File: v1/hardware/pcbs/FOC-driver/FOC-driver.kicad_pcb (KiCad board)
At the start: 4 copper layers, 100 x 100 mm, 225 parts, among them J1 HB9500M-9.5-2P, J10 S4B-XH-A, J11 S10B-XH-A, J12 S8B-XH-A, J13 S5B-XH-A, J14 S2B-XH-A, J16 S2B-XH-A, J2 HB9500-3, J3 B2B-XH-A, J4 B2B-XH-A, J5 B2B-XH-A, J6 B2B-XH-A, J7 S2B-XH-A, J8 S5B-XH-A, J9 S4B-XH-A, Q1 BSC093N15NS5, Q10 40N05, Q11 40N05, Q2 BSC093N15NS5, Q3 BSC093N15NS5, Q4 BSC093N15NS5, Q5 BSC093N15NS5, Q6 BSC093N15NS5, Q7 SP015N03BGHTO, Q8 40N05, Q9 40N05, SW1 TS-1088-AR02016, SW2 MSK22D18G2 125, Y1 C19674287, Y2 C48615

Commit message: new FOC driver connector placements and labels
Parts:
- removed LED3, LED4: C965799, LED_SMD:LED_0603_1608Metric
- removed R68: 300, Resistor_SMD:R_0402_1005Metric
- added J15: S5B-XH-A, Connector_JST:JST_XH_S5B-XH-A_1x05_P2.50mm_Horizontal, F.Cu at (-40.5, 28.0)
- R55: value 300 -> 10K
- moved F1 156.9 mm to (-42.0, -20.0)
- moved C37 150.2 mm to (-29.8, -28.0), turned to -90 degrees
- moved R55 85.9 mm to (-136.0, 154.6)
- moved C1 52.1 mm to (-152.8, -7.40)
- moved C14 52.1 mm to (-174.5, 136.1)
- moved C15 52.1 mm to (-174.5, 138.1)
- moved C19 52.1 mm to (-130.1, 120.6)
- moved C22 52.1 mm to (-138.0, 117.2)
- moved C23 52.1 mm to (-138.0, 122.1)
- moved C24 52.1 mm to (-163.5, 91.6)
- moved C25 52.1 mm to (-163.5, 93.6)
- moved C26 52.1 mm to (-130.1, 143.1)
- moved C27 52.1 mm to (-163.5, 95.6)
- moved C28 52.1 mm to (-163.5, 97.5)
- moved C29 52.1 mm to (-138.0, 139.6)
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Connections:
- net /LED1 renamed /LED
- MCU1 pad 26: /FAN2.EN -> /FAN1.EN
- MCU1 pad 30: /FAN3.PWM -> /DIP.CONF0
- MCU1 pad 33: /FAN4.PWM -> /DIP.CONF1
- MCU1 pad 34: /FAN4.EN -> /DIP.CONF2
- MCU1 pad 39: /DIP.CONF0 -> /FAN2.PWM
- MCU1 pad 40: /DIP.CONF1 -> /FAN3.PWM
- MCU1 pad 41: /DIP.CONF2 -> /FAN4.PWM
- MCU1 pad 49: /FDCAN.SILENT -> /DEBUG.SWDIO
- MCU1 pad 50: /FAN1.EN -> /DEBUG.SWCLK
- MCU1 pad 52: /LED3 -> /FAN4.EN
- MCU1 pad 53: /ENDSTOP1 -> /FAN3.EN
- MCU1 pad 54: /ENDSTOP2 -> /FAN2.EN
- MCU1 pad 56: /FAN2.PWM -> /DEBUG.SWO
- MCU1 pad 62: /FAN3.EN -> /ENDSTOP2
- MCU1 pad 8: /LED2 -> /ENDSTOP1
- R54 pad 1: /LED2 -> +3.3V
- R55 pad 1: /LED3 -> /FDCAN.SILENT
- R55 pad 2: Net-(LED3-A) -> GND
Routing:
- net GND: track 1.05 -> 15.1 mm, vias 1 -> 5
- net /power/VMOT_UNFUSED: track 11.3 -> 23.4 mm
- net /power/VMOT_UNFILTERED: track 9.73 -> 3.17 mm
- net /power/VMOT_GATE: track 11.6 -> 12.5 mm
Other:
- board text added: "+"
- board text added: "-"
- board text added: "- FAN +"
- board text added: "GND 5V A+A- B+B- Z+Z- ENCODER ABZ"
- board text added: "GND 5V CK+CK- CS+CS- MO+MO- MI+MI- ENCODER SPI"
- board text added: "GND 5V S+S- ENDSTOP1"
- board text added: "GND 5V S+S- ENDSTOP2"
- board text added: "GND CAN+CAN- CAN-CAN+ CAN-FD"
- board text added: "GND NRST CLK DIO SWO SW DEBUG"
- board text added: "GND TX+TX- RX+RX- RS422"
- board text added: "MOTOR TH"

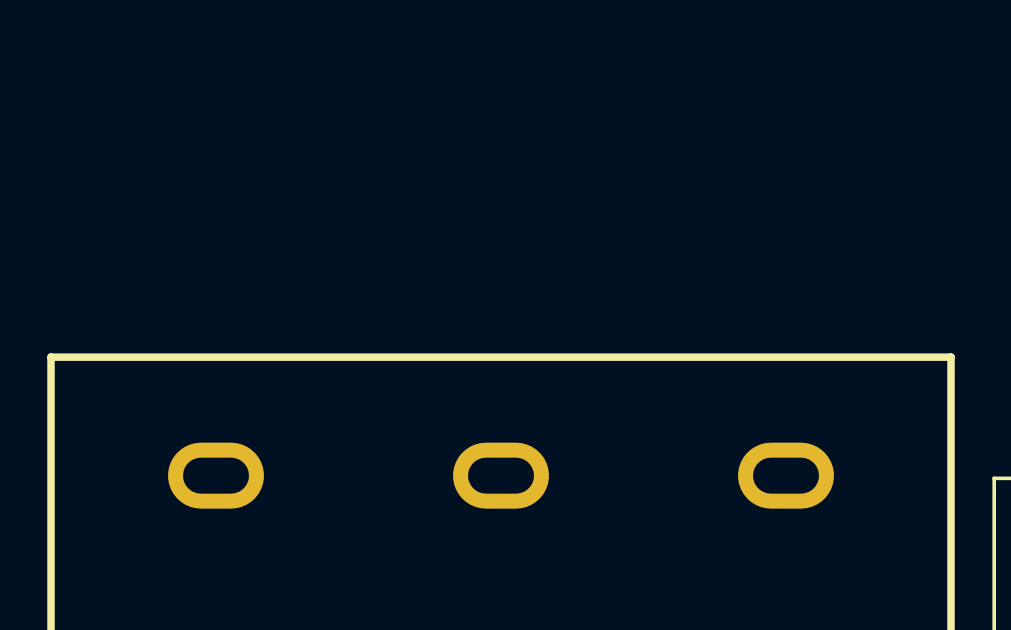
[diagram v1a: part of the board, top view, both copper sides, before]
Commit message: new FOC driver inverter out label
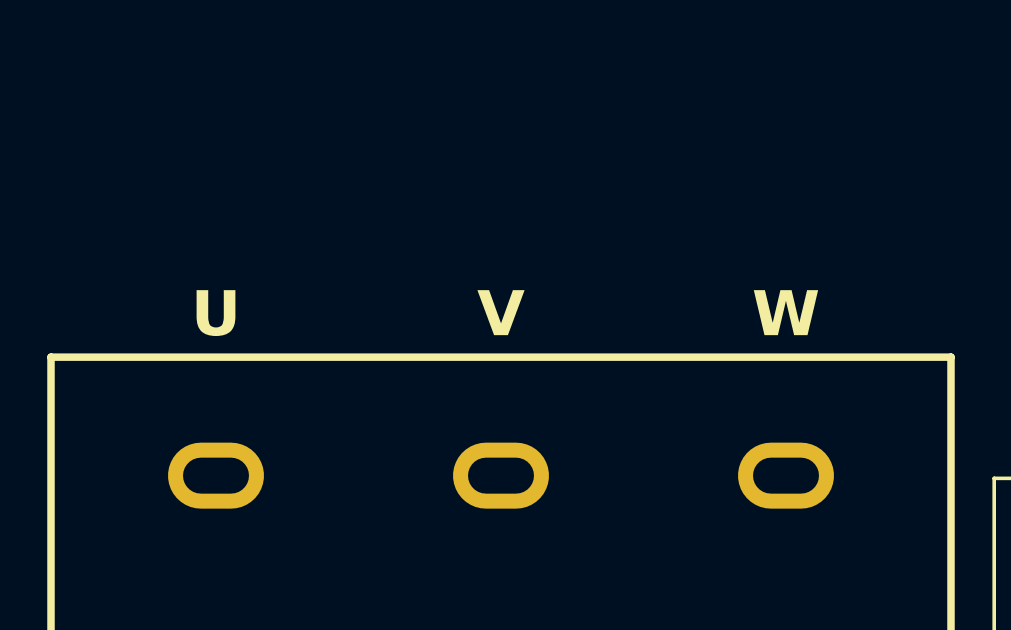
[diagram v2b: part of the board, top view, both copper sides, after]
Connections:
- J2 pad 1: /W_POWER -> /U_POWER
- J2 pad 3: /U_POWER -> /W_POWER
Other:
- board text added: "U"
- board text added: "V"
- board text added: "W"
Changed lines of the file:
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@@
 			(layers "*.Cu" "*.Mask")
 			(remove_unused_layers no)
-			(net 32 "/W_POWER")
+			(net 30 "/U_POWER")
 			(pinfunction "1")
 			(pintype "passive")
@@
 			(layers "*.Cu" "*.Mask")
 			(remove_unused_layers no)
-			(net 30 "/U_POWER")
+			(net 32 "/W_POWER")
 			(pinfunction "3")
 			(pintype "passive")
@@
 		(layer "Edge.Cuts")
 	)
+	(gr_text "V"
+		(at -2 33.5 0)
+		(layer "F.SilkS")
+		(effects
+			(font
+				(size 1.5 1.5)
+				(thickness 0.3)
+				(bold yes)
+			)
+			(justify bottom)
+		)
+	)
 	(gr_text "GND 5V A+A- B+B- Z+Z-\nENCODER ABZ"
 		(at 39 24.75 90)
@@
 				(bold yes)
 			)
+			(justify bottom)
+		)
+	)
+	(gr_text "W"
+		(at 7.5 33.5 0)
+		(layer "F.SilkS")
+		(effects
+			(font
+				(size 1.5 1.5)
+				(thickness 0.3)
+				(bold yes)
+			)
+			(justify bottom)
+		)
+	)
+	(gr_text "U"
+		(at -11.5 33.5 0)
+		(layer "F.SilkS")
+		(effects
+			(font
+				(size 1.5 1.5)
+				(thickness 0.3)
+				(bold yes)
+			)

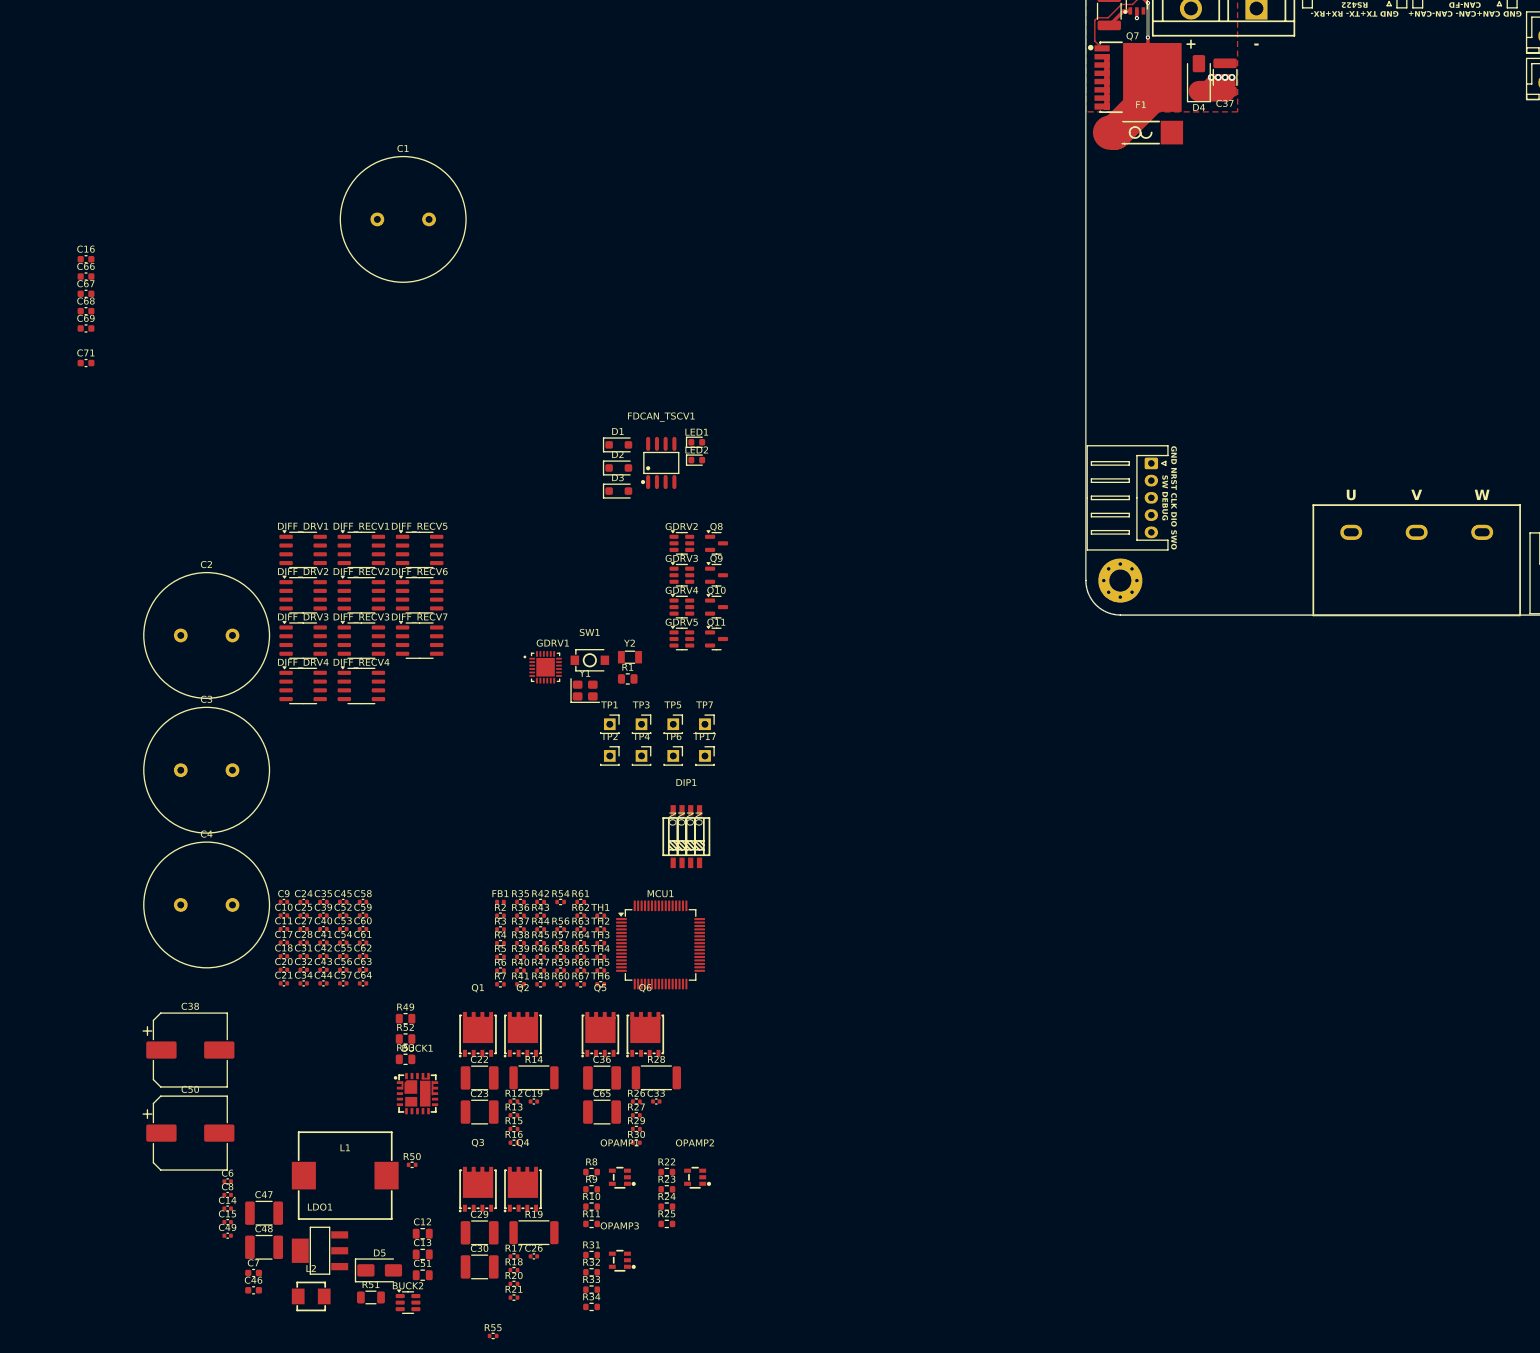
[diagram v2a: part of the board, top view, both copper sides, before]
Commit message: new FOC driver power step-down layout and inverter layout
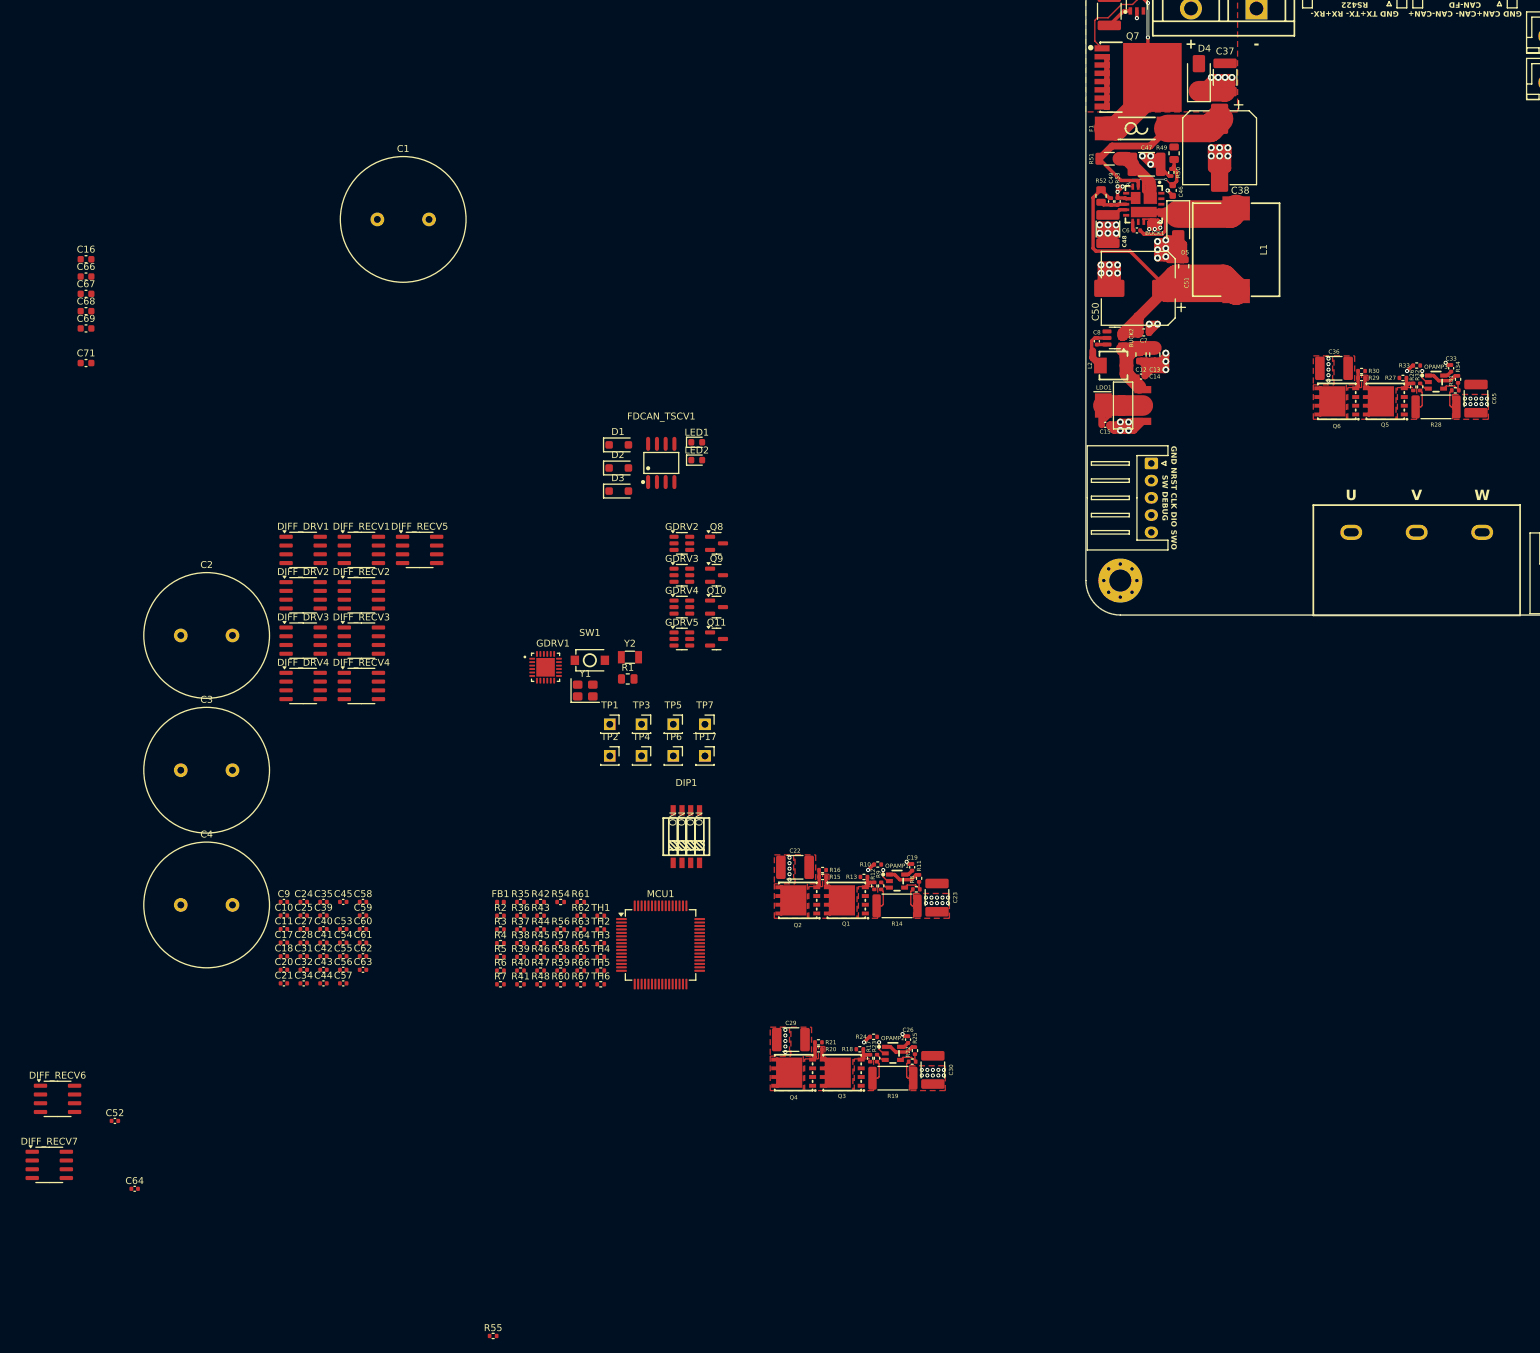
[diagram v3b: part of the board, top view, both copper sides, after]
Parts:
- R10, R11, R22, R23, R24, R25, R31, R32, R33, R34, R8, R9: footprint Resistor_SMD:R_0603_1608Metric -> Resistor_SMD:R_0402_1005Metric
- R52: footprint Resistor_SMD:R_0805_2012Metric -> footprints:R_0805_2012Metric
- R53: footprint Resistor_SMD:R_0805_2012Metric -> Resistor_SMD:R_0402_1005Metric
- moved C46 208.0 mm to (-37.4, -11.6), turned to -90 degrees
- moved C47 198.9 mm to (-41.2, -15.4)
- moved C38 198.6 mm to (-30.6, -17.8), turned to -90 degrees
- moved C49 197.3 mm to (-46.4, -10.0), turned to -90 degrees
- moved R51 196.9 mm to (-46.6, -16.2)
- moved C48 191.9 mm to (-46.8, -6.00), turned to -90 degrees
- moved C6 190.9 mm to (-42.6, -5.80)
- moved D5 190.9 mm to (-36.6, -6.60), turned to -90 degrees
- moved C7 187.9 mm to (-41.6, 9.00)
- moved L1 186.4 mm to (-28.2, -3.00), turned to -90 degrees
- moved C50 184.2 mm to (-42.4, 2.60), turned to 180 degrees
- moved R34 184.2 mm to (4.00, 15.8), turned to 90 degrees
- moved C51 183.4 mm to (-35.8, -0.60), turned to 90 degrees
- moved R50 181.3 mm to (-37.6, -14.2), turned to -90 degrees
- moved R33 179.7 mm to (-2.00, 13.8)
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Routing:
- net GND: track 15.1 -> 214.5 mm, vias 5 -> 103
- net +12V: track 0.00 -> 59.9 mm
- net VMOT: track 0.00 -> 27.6 mm
- net /power/BUCK_SW: track 0.00 -> 19.8 mm
- net +3.3V: track 0.00 -> 16.8 mm
- net /power/BUCK_ISEN: track 0.00 -> 16.0 mm
- net +5V: track 0.00 -> 15.8 mm
- net /power/BUCK_EN: track 0.00 -> 13.8 mm, vias 0 -> 2
- net Net-(BUCK2-SW): track 0.00 -> 6.49 mm
- net /W_I_SENSE: track 0.00 -> 4.91 mm
- net /U_I_SENSE: track 0.00 -> 4.91 mm
- net /V_I_SENSE: track 0.00 -> 4.91 mm
- net /power/BUCK_FB: track 0.00 -> 3.86 mm
- net Net-(OPAMP2-IN-): track 0.00 -> 3.76 mm
- net Net-(OPAMP3-IN-): track 0.00 -> 3.76 mm
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- added copper zone on F.Cu, net /U-power-phase/BRIDGE_GND
- added copper zone on F.Cu, net /U_POWER
- added copper zone on F.Cu, net /V-power-phase/BRIDGE_GND
- added copper zone on F.Cu, net /V_POWER
- added copper zone on F.Cu, net /W-power-phase/BRIDGE_GND
- added copper zone on F.Cu, net /W_POWER
- added copper zone on F.Cu, net GND
- added copper zone on F.Cu, net VMOT
